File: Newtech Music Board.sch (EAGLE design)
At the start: 51 parts, among them J1 SS-30_BOARD_CONNECTOR, U1 74LS10N, U2 74LS174N, U3 4050N, U4 4069N, U5 LM386N-1

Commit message: Updated Speaker and incorrect resistor value
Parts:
- removed SP1: AL201P, buzzer:AL201P
- added LS1: AST-01508MR-R, AST-01508MR-R:AST-01508MR-R
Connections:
- net GND: now also LS1.2; no longer SP1.2
- net N$48: now also LS1.1; no longer SP1.1

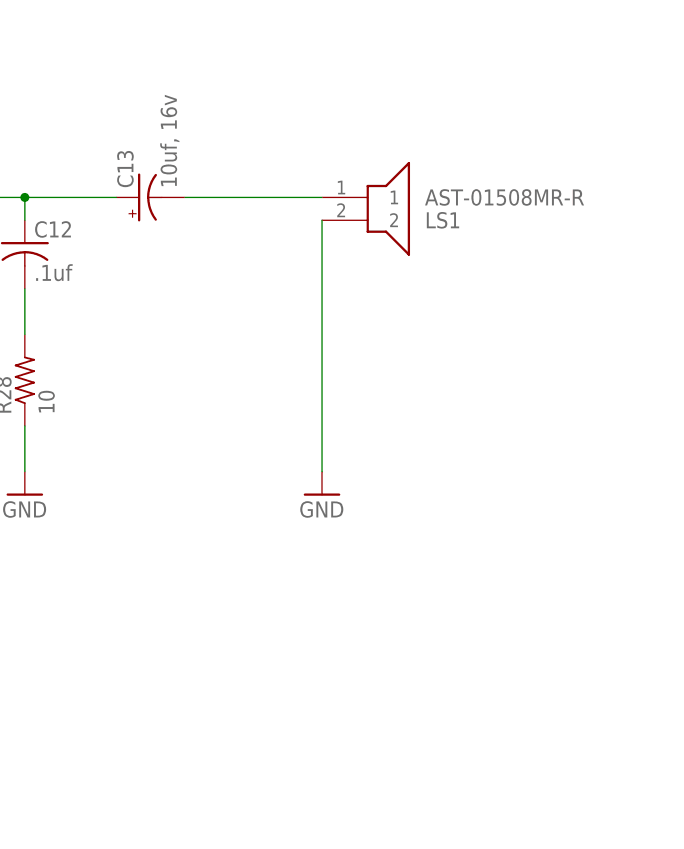
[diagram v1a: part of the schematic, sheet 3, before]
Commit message: Added headphone jack out
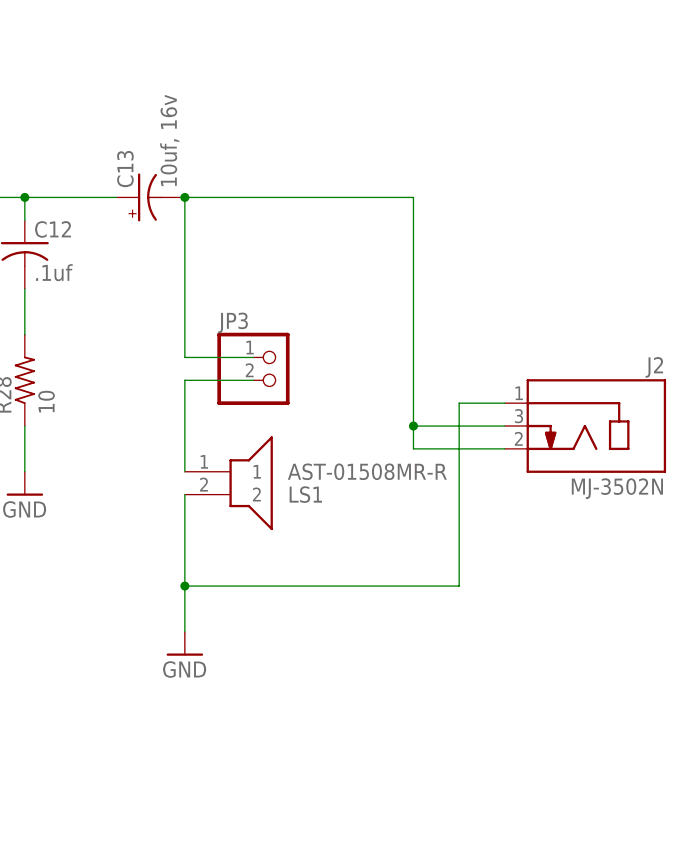
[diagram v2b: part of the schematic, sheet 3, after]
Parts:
- added J2: MJ-3502N, MJ-3502N:MJ-3502N
- added JP3: (no value), pinhead:PINHD-1X2
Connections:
- new net N$15: JP3.2, LS1.1
- net GND: now also J2.1
- net N$48: now also J2.2, J2.3, JP3.1; no longer LS1.1
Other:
- moved on the sheet: LS1
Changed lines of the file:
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@@
 <class number="0" name="default" width="0" drill="0">
+</class>
+<class number="1" name="POWER" width="0.762" drill="0">
 </class>
 </classes>
@@
 <part name="GND10" library="supply1" deviceset="GND" device=""/>
 <part name="LS1" library="AST-01508MR-R" deviceset="AST-01508MR-R" device=""/>
+<part name="JP3" library="pinhead" library_urn="urn:adsk.eagle:library:325" deviceset="PINHD-1X2" device="" package3d_urn="urn:adsk.eagle:package:22435/2"/>
+<part name="J2" library="MJ-3502N" deviceset="MJ-3502N" device=""/>
 </parts>
 <sheets>
@@
 </segment>
 </net>
-<net name="+8V" class="0">
+<net name="+8V" class="1">
 <segment>
 <pinref part="J1" gate="G$2" pin="+8V@2"/>
@@
 <attribute name="VALUE" x="137.16" y="81.28" size="1.778" layer="96"/>
 </instance>
-<instance part="GND9" gate="1" x="172.72" y="83.82" smashed="yes">
-<attribute name="VALUE" x="170.18" y="81.28" size="1.778" layer="96"/>
-</instance>
-<instance part="LS1" gate="G$1" x="172.72" y="114.3" smashed="yes" rot="MR180">
-<attribute name="NAME" x="184.15" y="114.3" size="1.778" layer="95" rot="MR180" align="center-left"/>
-<attribute name="VALUE" x="184.15" y="116.84" size="1.778" layer="96" rot="MR180" align="center-left"/>
+<instance part="GND9" gate="1" x="157.48" y="66.04" smashed="yes">
+<attribute name="VALUE" x="154.94" y="63.5" size="1.778" layer="96"/>
+</instance>
+<instance part="LS1" gate="G$1" x="157.48" y="83.82" smashed="yes" rot="MR180">
+<attribute name="NAME" x="168.91" y="83.82" size="1.778" layer="95" rot="MR180" align="center-left"/>
+<attribute name="VALUE" x="168.91" y="86.36" size="1.778" layer="96" rot="MR180" align="center-left"/>
+</instance>
+<instance part="JP3" gate="G$1" x="167.64" y="96.52" smashed="yes">
+<attribute name="NAME" x="161.29" y="102.235" size="1.778" layer="95"/>
+<attribute name="VALUE" x="161.29" y="91.44" size="1.778" layer="96"/>
+</instance>
+<instance part="J2" gate="G$1" x="203.2" y="91.44" smashed="yes" rot="MR0">
+<attribute name="NAME" x="210.83351875" y="97.29236875" size="1.781159375" layer="95" rot="MR0"/>
+<attribute name="VALUE" x="210.82108125" y="83.81891875" size="1.77825" layer="96" rot="MR0"/>
 </instance>
 </instances>
@@
 <segment>
 <pinref part="GND9" gate="1" pin="GND"/>
-<wire x1="172.72" y1="114.3" x2="172.72" y2="86.36" width="0.1524" layer="91"/>
+<wire x1="157.48" y1="83.82" x2="157.48" y2="73.66" width="0.1524" layer="91"/>
 <pinref part="LS1" gate="G$1" pin="2"/>
+<pinref part="J2" gate="G$1" pin="1"/>
+<wire x1="157.48" y1="73.66" x2="157.48" y2="68.58" width="0.1524" layer="91"/>
+<wire x1="193.04" y1="93.98" x2="187.96" y2="93.98" width="0.1524" layer="91"/>
+<wire x1="187.96" y1="93.98" x2="187.96" y2="73.66" width="0.1524" layer="91"/>
+<wire x1="187.96" y1="73.66" x2="157.48" y2="73.66" width="0.1524" layer="91"/>
+<junction x="157.48" y="73.66"/>
 </segment>
 </net>
@@
 </segment>
 </net>
-<net name="+8V" class="0">
+<net name="+8V" class="1">
 <segment>
 <wire x1="30.48" y1="78.74" x2="33.02" y2="76.2" width="0.1524" layer="91"/>
@@
 <segment>
 <pinref part="C13" gate="G$1" pin="-"/>
-<wire x1="157.48" y1="116.84" x2="172.72" y2="116.84" width="0.1524" layer="91"/>
-<pinref part="LS1" gate="G$1" pin="1"/>
+<wire x1="157.48" y1="116.84" x2="157.48" y2="99.06" width="0.1524" layer="91"/>
+<pinref part="JP3" gate="G$1" pin="1"/>
+<wire x1="157.48" y1="99.06" x2="165.1" y2="99.06" width="0.1524" layer="91"/>
+<wire x1="157.48" y1="116.84" x2="182.88" y2="116.84" width="0.1524" layer="91"/>
+<junction x="157.48" y="116.84"/>
+<wire x1="182.88" y1="116.84" x2="182.88" y2="91.44" width="0.1524" layer="91"/>
+<pinref part="J2" gate="G$1" pin="3"/>
+<wire x1="182.88" y1="91.44" x2="193.04" y2="91.44" width="0.1524" layer="91"/>
+<pinref part="J2" gate="G$1" pin="2"/>
+<wire x1="193.04" y1="88.9" x2="182.88" y2="88.9" width="0.1524" layer="91"/>
+<wire x1="182.88" y1="88.9" x2="182.88" y2="91.44" width="0.1524" layer="91"/>
+<junction x="182.88" y="91.44"/>
 </segment>
 </net>
@@
 <pinref part="R28" gate="G$1" pin="2"/>
 <wire x1="139.7" y1="106.68" x2="139.7" y2="101.6" width="0.1524" layer="91"/>
+</segment>
+</net>
+<net name="N$15" class="0">
+<segment>
+<pinref part="LS1" gate="G$1" pin="1"/>
+<wire x1="157.48" y1="96.52" x2="157.48" y2="86.36" width="0.1524" layer="91"/>
+<pinref part="JP3" gate="G$1" pin="2"/>
+<wire x1="165.1" y1="96.52" x2="157.48" y2="96.52" width="0.1524" layer="91"/>
 </segment>
 </net>
@@
 </schematic>
 </drawing>
+<compatibility>
+<note version="8.2" severity="warning">
+Since Version 8.2, EAGLE supports online libraries. The ids
+of those online libraries will not be understood (or retained)
+with this version.
+</note>
+<note version="8.3" severity="warning">
+Since Version 8.3, EAGLE supports URNs for individual library
+assets (packages, symbols, and devices). The URNs of those assets
+will not be understood (or retained) with this version.
+</note>
+<note version="8.3" severity="warning">
+Since Version 8.3, EAGLE supports the association of 3D packages
+with devices in libraries, schematics, and board files. Those 3D
+packages will not be understood (or retained) with this version.
+</note>
+</compatibility>
 </eagle>

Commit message: Put real speaker on
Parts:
- removed LS1: AST-01508MR-R, AST-01508MR-R:AST-01508MR-R
- removed R14: 330K, rcl:R-US_0204/7
- added C14: .0022uF, rcl:C-US025-025X050
- added JP4: (no value), pinhead:PINHD-1X2
- added R29: 330K, rcl:R-US_0204/7
- added VR2: 3362P-1-253TLF, 3362P-1-253TLF:3362P-1-253TLF
- C13: value 10uf, 16v -> 220uF,25v; device rcl:CPOL-USE2.5-6 -> rcl:CPOL-USE25-9AXIAL
- R13: value 367K -> 357K
- R27: value 5K -> 2M; device resistor:R-TRIMM43P -> rcl:R-US_0204/7
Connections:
- removed net N$30: C4.2, R14.1
- new net N$51: C5.1, R29.1
- net DAC_OUT: now also C4.2; no longer R14.2
- net GND: now also C14.2, JP4.2, VR2.CCW; no longer LS1.2, R27.E
- net LPF_BYPASS: now also R27.2; no longer JP1.1
- net LPF_OUT: now also C14.1, U5.+IN, VR2.CW, VR2.WIPER; no longer R27.A
- net N$15: now also JP4.1; no longer LS1.1
- net N$32: now also R29.2; no longer C5.1
- net N$39: now also JP1.1, R27.1; no longer R27.S, U5.+IN

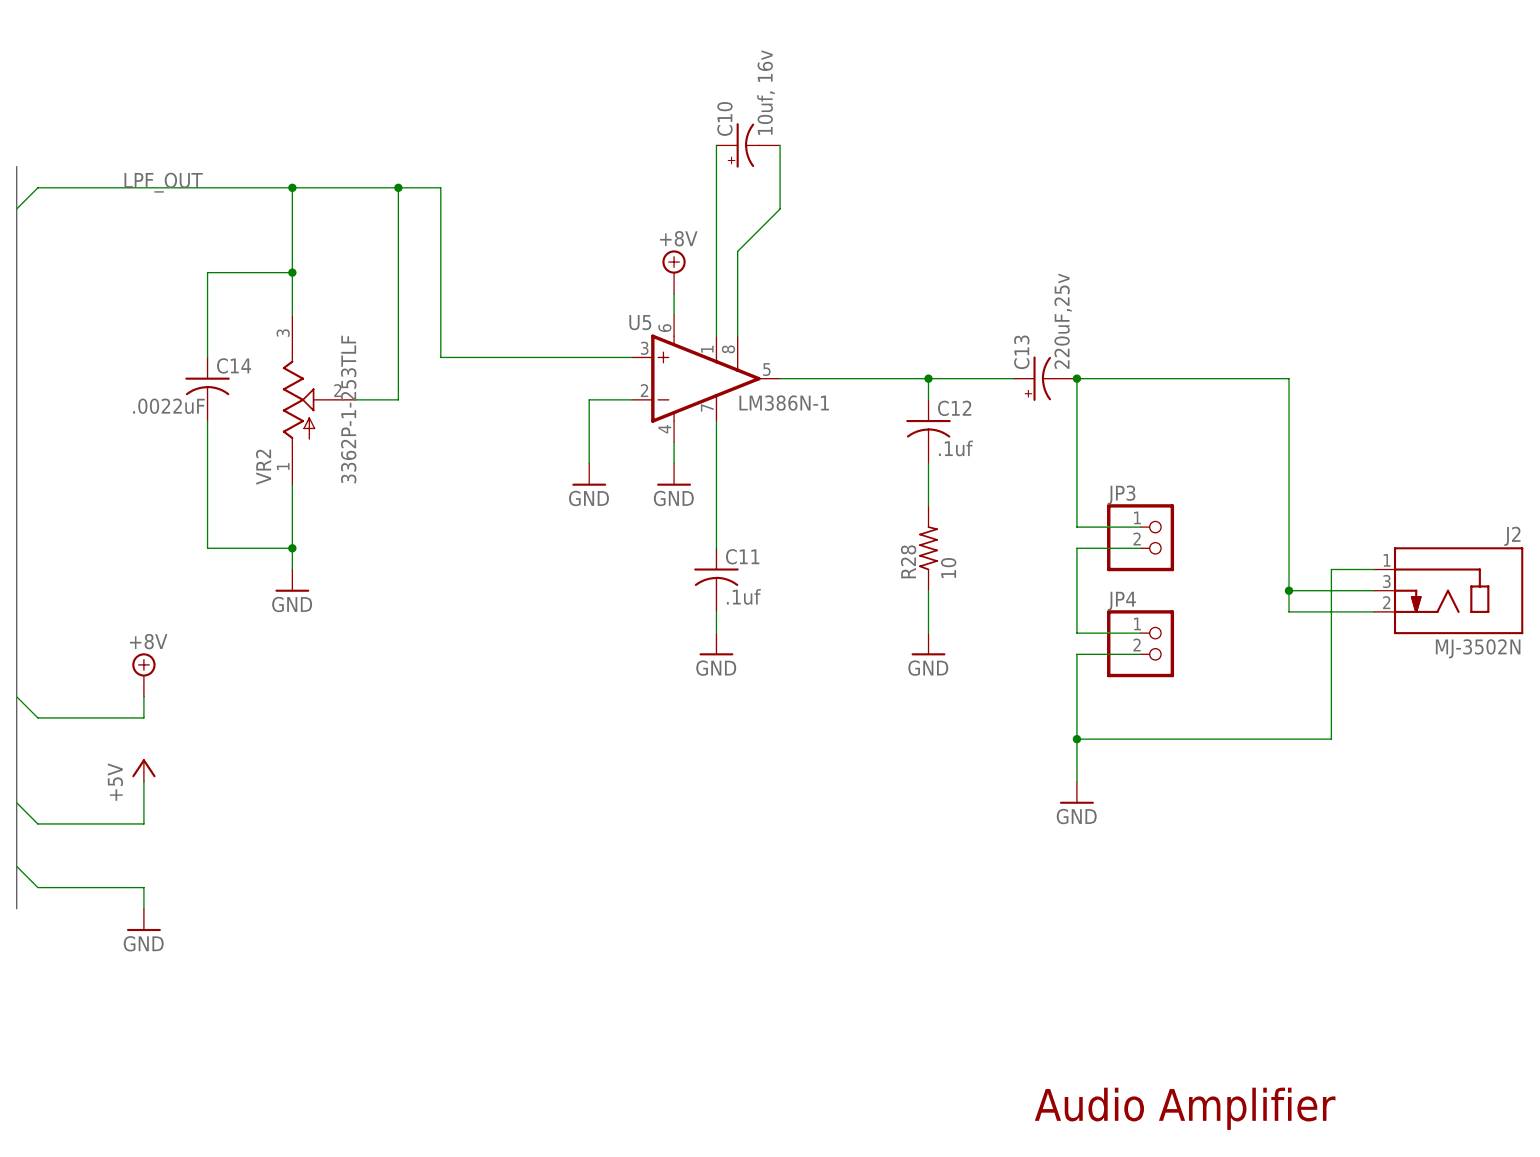
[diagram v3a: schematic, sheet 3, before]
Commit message: Matched the circuit to the S-100 Board
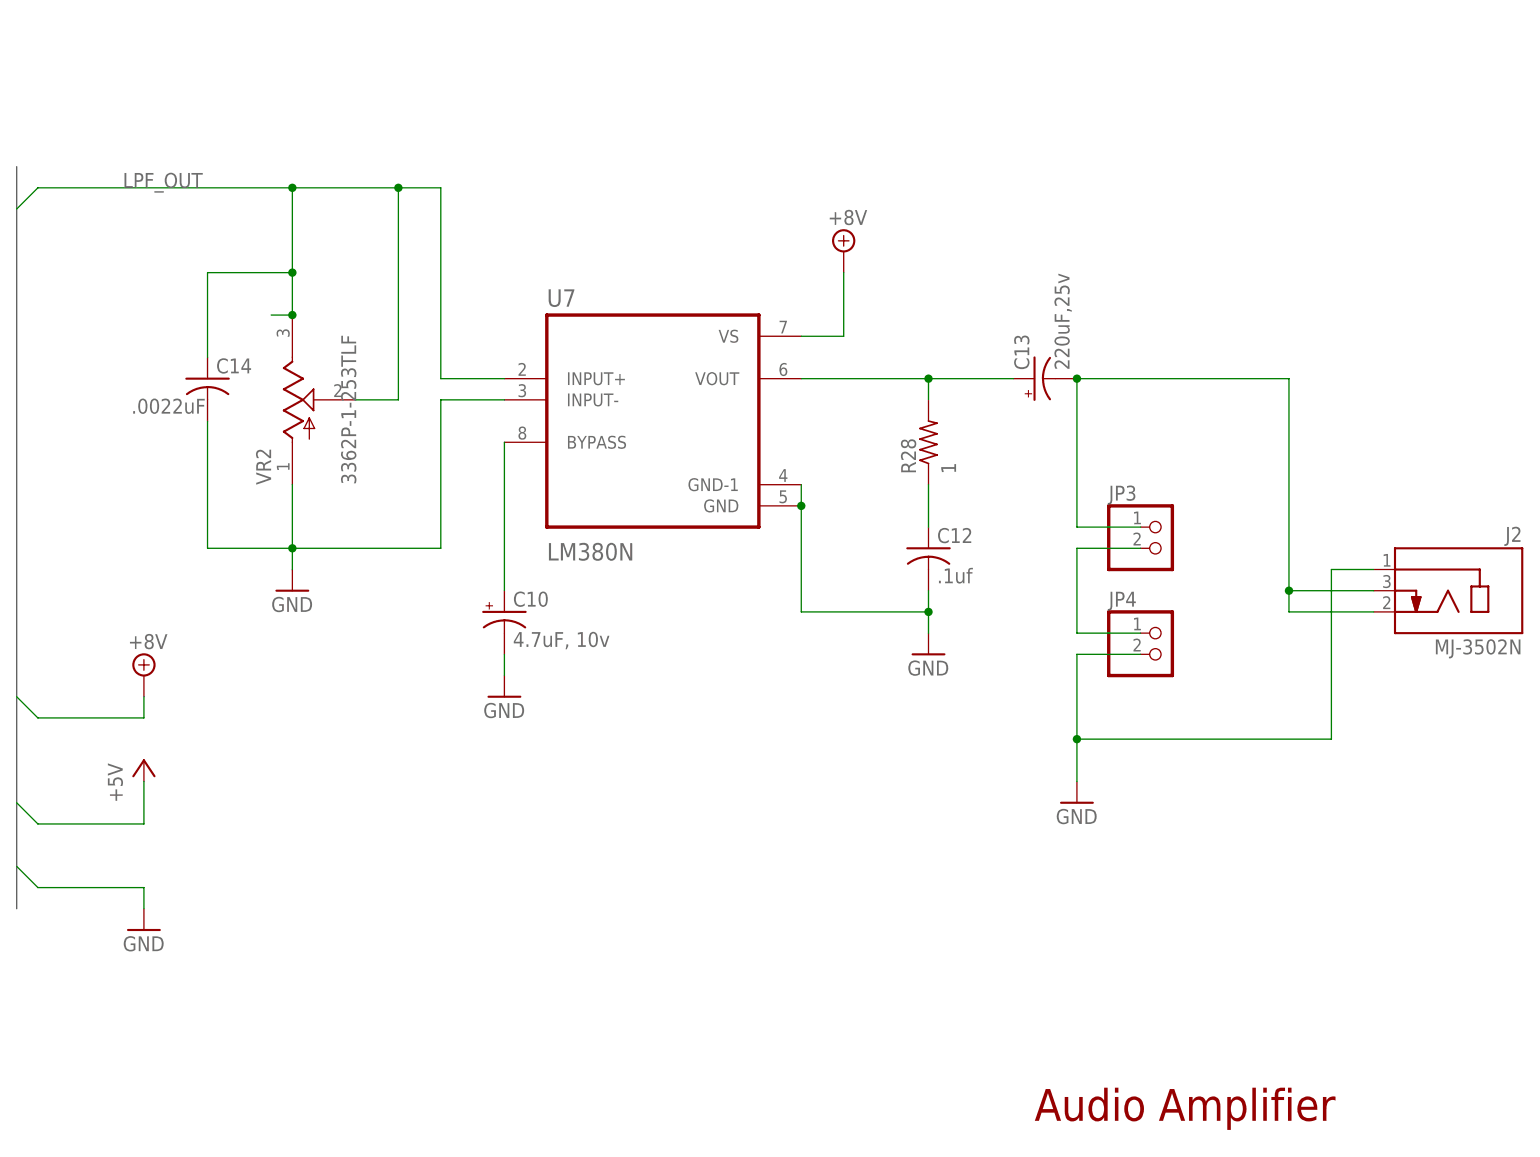
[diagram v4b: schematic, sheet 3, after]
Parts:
- removed C11: .1uf, rcl:C-US025-025X050
- removed U5: LM386N-1, linear:LM386N-1
- removed VR1: 7805, v-reg:78XXL
- added U6: 78L05, 78L05ACZ:78L05ACZ
- added U7: LM380N, LM380N-8_NOPB:LM380N-8/NOPB
- C1: value 10uf, 16v -> 1uF, 35v
- C10: value 10uf, 16v -> 4.7uF, 10v
- R28: value 10 -> 1; device rcl:R-US_0204/7 -> rcl:R-US_0207/12
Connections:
- removed net N$44: C11.1, U5.BYPASS
- removed net N$46: C10.-, U5.GAIN@2
- removed net N$50: C12.2, R28.2
- new net N$30: C10.+, U7.BYPASS
- net +5V: now also U6.VO; no longer VR1.OUT
- net +8V: now also U6.VI, U7.VS; no longer U5.VS, VR1.IN
- net GND: now also C10.-, C12.2, U6.GND, U7.GND, U7.GND-1, U7.INPUT-; no longer C11.2, R28.1, U5.-IN, U5.GND, VR1.GND
- net LPF_OUT: now also U7.INPUT+; no longer U5.+IN
- net N$36: now also C12.1, R28.1; no longer C10.+, U5.GAIN@1
- net N$47: now also R28.2, U7.VOUT; no longer C12.1, U5.OUT
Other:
- moved on the sheet: C10, C12, R28

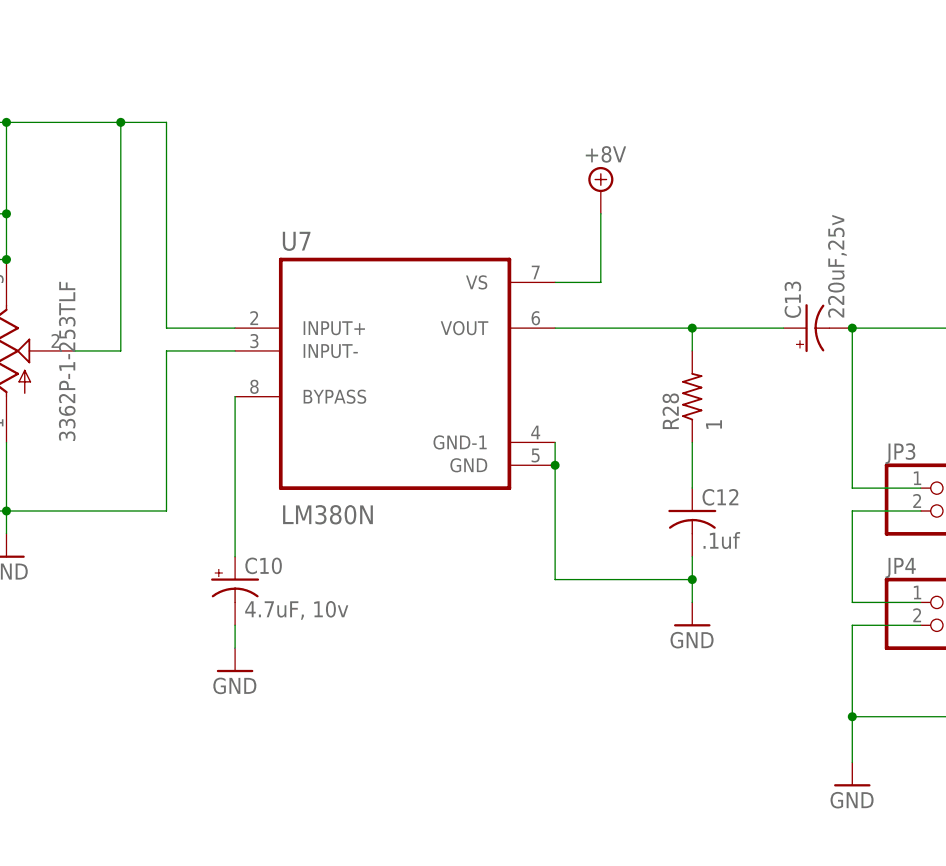
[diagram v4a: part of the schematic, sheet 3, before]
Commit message: Put back the LM386
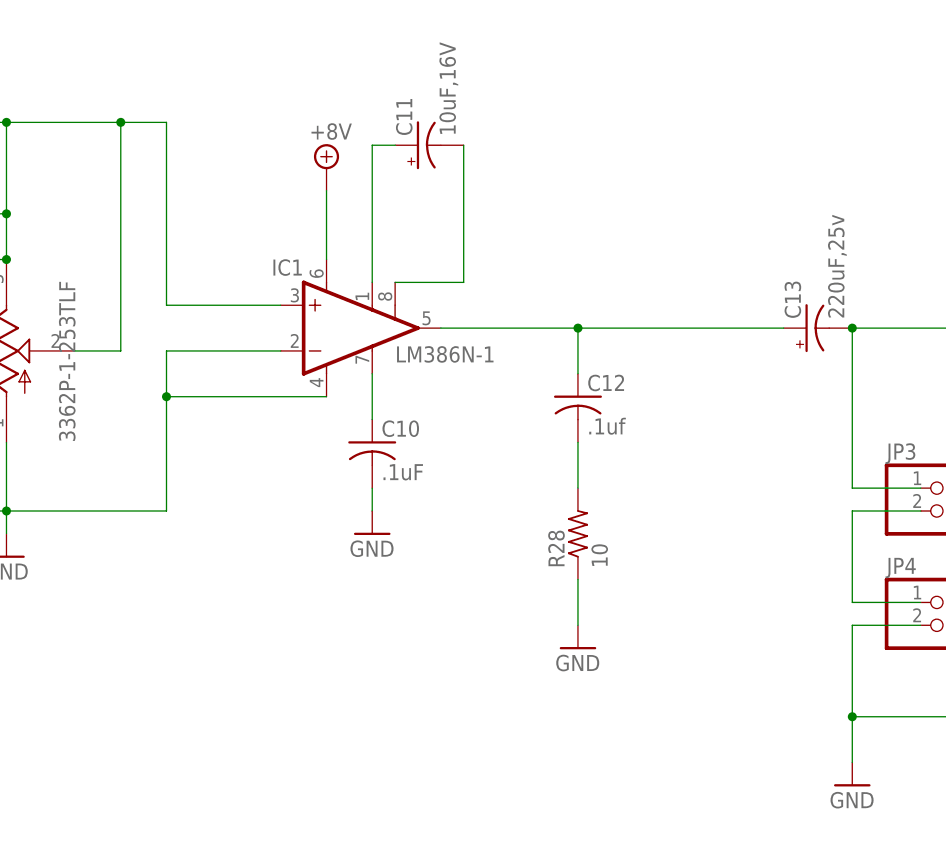
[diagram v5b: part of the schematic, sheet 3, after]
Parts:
- removed U7: LM380N, LM380N-8_NOPB:LM380N-8/NOPB
- added C11: 10uF,16V, rcl:CPOL-USE2.5-6
- added IC1: LM386N-1, linear:LM386N-1
- C10: value 4.7uF, 10v -> .1uF; device rcl:CPOL-USE2.5-6 -> rcl:C-US025-025X050
- R28: value 1 -> 10; device rcl:R-US_0207/12 -> rcl:R-US_0204/7
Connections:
- new net N$46: C11.+, IC1.GAIN@1
- new net N$50: C11.-, IC1.GAIN@2
- net +8V: now also IC1.VS; no longer U7.VS
- net GND: now also C10.2, IC1.-IN, IC1.GND, R28.1; no longer C10.-, C12.2, U7.GND, U7.GND-1, U7.INPUT-
- net LPF_OUT: now also IC1.+IN; no longer U7.INPUT+
- net N$30: now also C10.1, IC1.BYPASS; no longer C10.+, U7.BYPASS
- net N$36: now also C12.2, R28.2; no longer C12.1, R28.1
- net N$47: now also C12.1, IC1.OUT; no longer R28.2, U7.VOUT
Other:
- moved on the sheet: C12, R28
